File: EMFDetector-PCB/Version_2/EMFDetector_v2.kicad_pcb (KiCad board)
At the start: 2 copper layers, 50 x 50 mm, 23 parts, among them J1 PHONO, P2 BATT, P3 PCB, P4 LOGO1, P5 LOGO2, SW1 PWR, U1 OPA2134

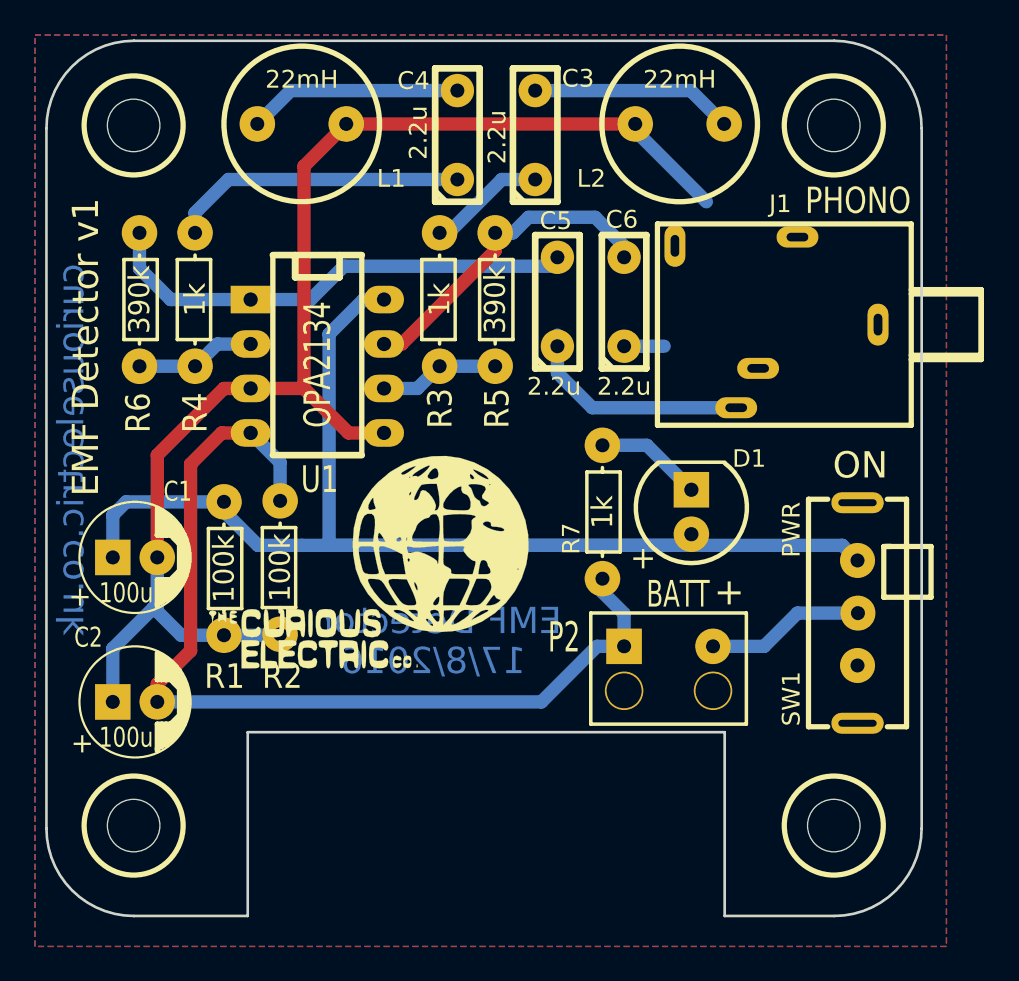
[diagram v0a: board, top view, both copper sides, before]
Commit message: New version of PCB built for new kicad version
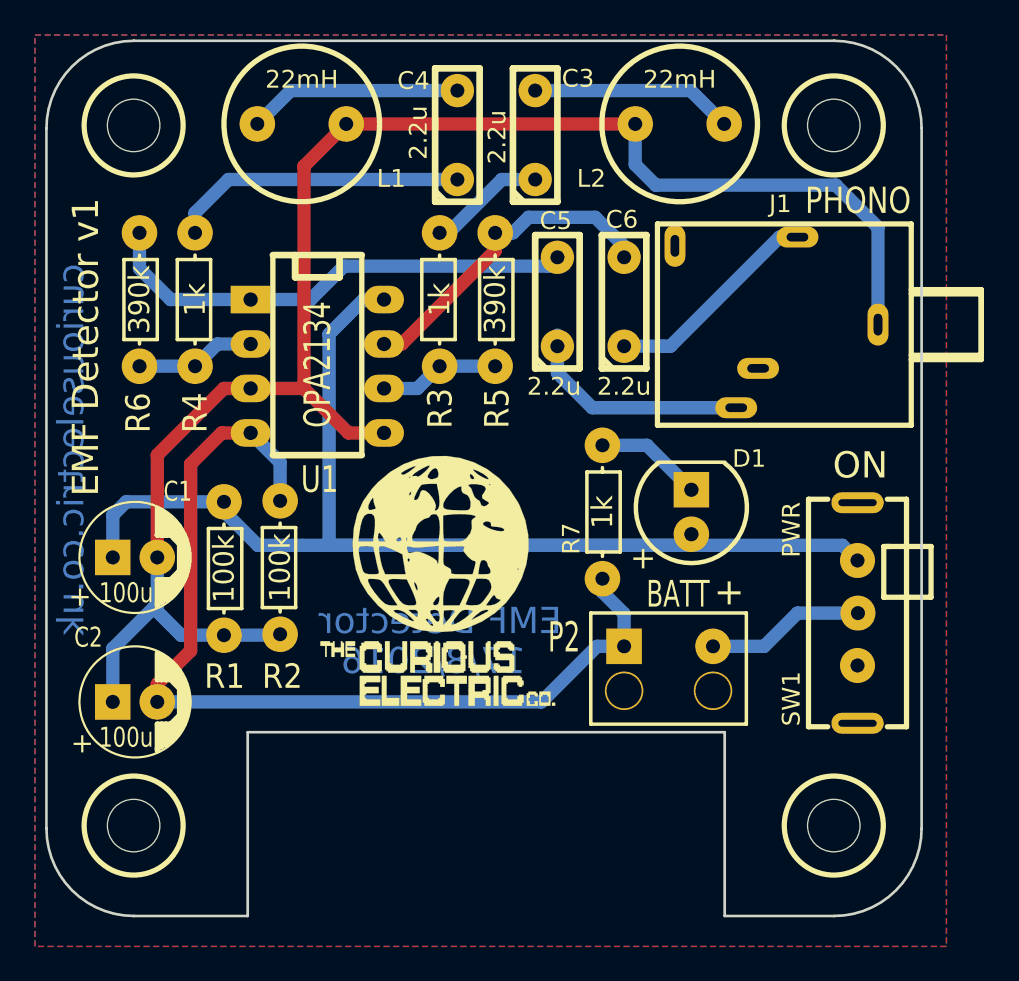
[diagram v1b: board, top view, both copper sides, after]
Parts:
- P4: footprint CuriousElectric3:CuriousElectric_flat_12mm -> CuriousElectric3:TCEC_Words_13mm
- moved P4 0.28 mm to (135.4, 129.0)
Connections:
- J1 pad 1: Net-(C6-Pad1) -> GND
- J1 pad 2: GND -> Net-(C6-Pad1)
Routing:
- net GND: track 78.0 -> 95.1 mm
- net Net-(C6-Pad1): track 2.29 -> 12.9 mm
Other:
- rule pad_to_mask_clearance: 0.2 -> 0
